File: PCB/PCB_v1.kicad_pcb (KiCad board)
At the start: 2 copper layers, 80 x 40 mm, 11 parts, among them J1 Accelerometer, J2 Flysky FS2A Receiver, J3 DC-DC, J4 Battery Left, J5 Battery Right, J6 ESC_Left, J7 ESC_Right, U1 Teensy4.0

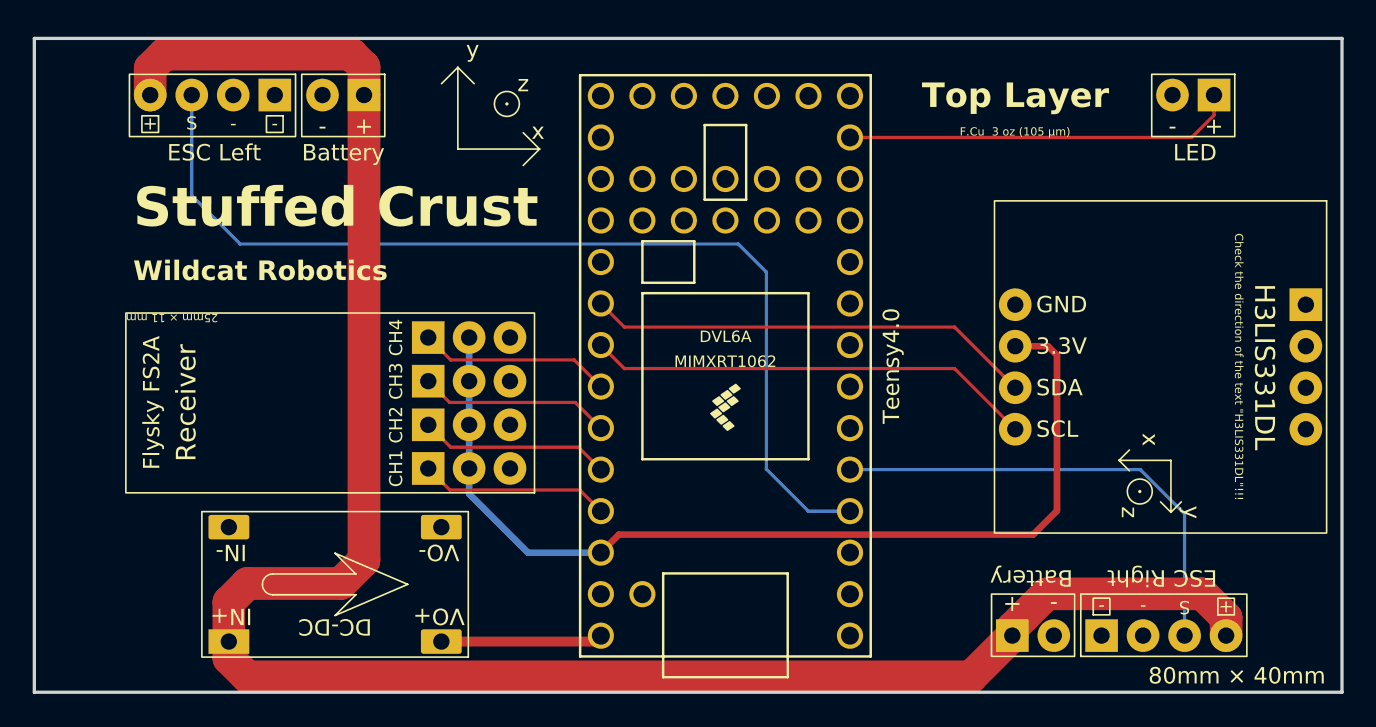
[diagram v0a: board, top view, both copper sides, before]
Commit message: Separate GND (for signal) and GND_BT (for high current); make bigger holes for high current wires
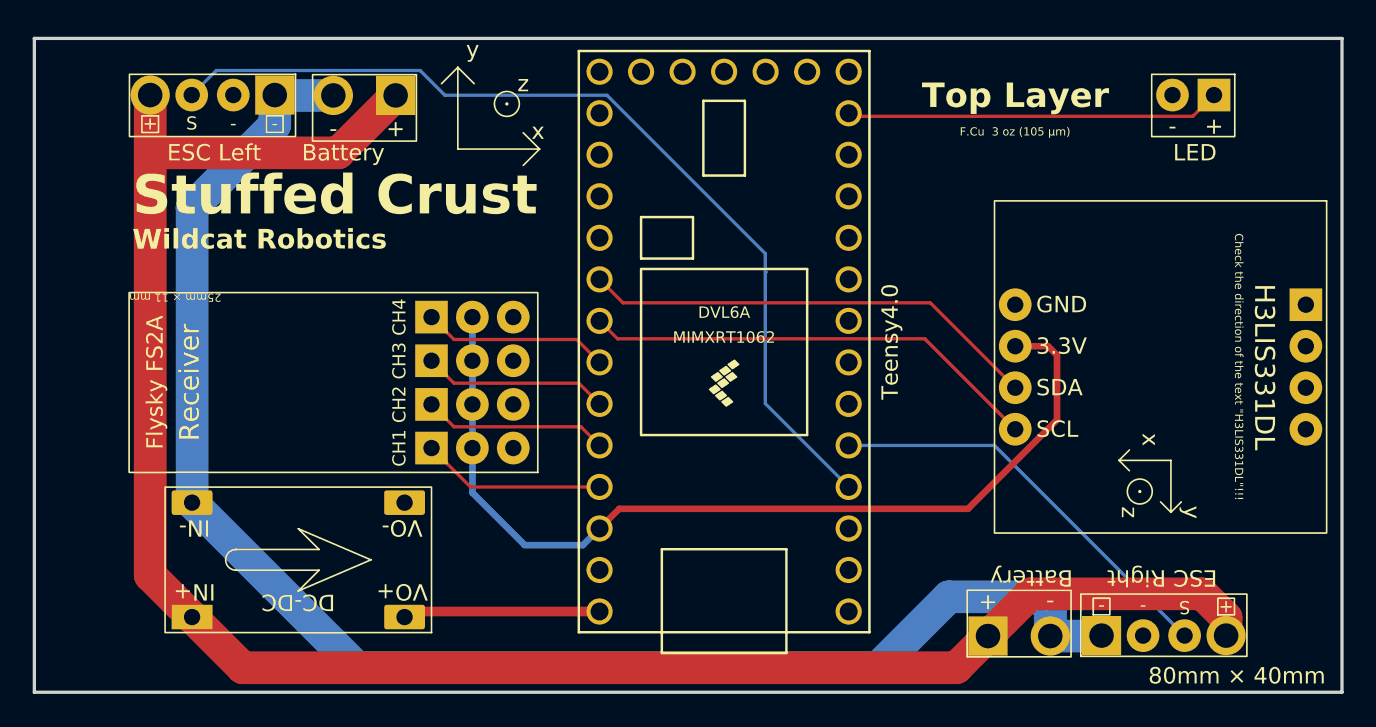
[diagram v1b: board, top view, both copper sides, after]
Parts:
- J4, J5: footprint Stuffed Crust:Battery_or_LED -> Stuffed Crust:Battery
- J8: renamed from Je; footprint Stuffed Crust:Battery_or_LED -> Stuffed Crust:LED
- moved J3 2.70 mm to (156.2, 91.9)
- moved J4 1.94 mm to (163.4, 62.2)
- moved J5 1.49 mm to (197.1, 97.8)
- moved U1 1.48 mm to (182.2, 78.5)
- moved J2 1.27 mm to (170.8, 86.5)
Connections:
- J3 pad 2: /GND -> /GND_BT
- J4 pad 2: /GND -> /GND_BT
- J5 pad 2: /GND -> /GND_BT
- J6 pad 1: /GND -> /GND_BT
- J7 pad 1: /GND -> /GND_BT
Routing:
- net /GND_BT: track 0.00 -> 94.3 mm
- net /12V: track 123.9 -> 117.6 mm
- net /S_ESC_Left_2: track 61.5 -> 56.8 mm
- net /S_ESC_Right_3: track 29.0 -> 25.4 mm
- net /3.3V: track 60.4 -> 57.8 mm
- net /5V: track 9.91 -> 12.1 mm
- net /LED: track 24.1 -> 23.0 mm
- net /SCL_19: track 27.5 -> 28.2 mm
- net /SDA_18: track 27.5 -> 28.2 mm
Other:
- board text added: "B.Cu 3 oz (105 μm)"
- board text removed: "B.Cu 1 oz (35 μm)"

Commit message: Fix the GND fill
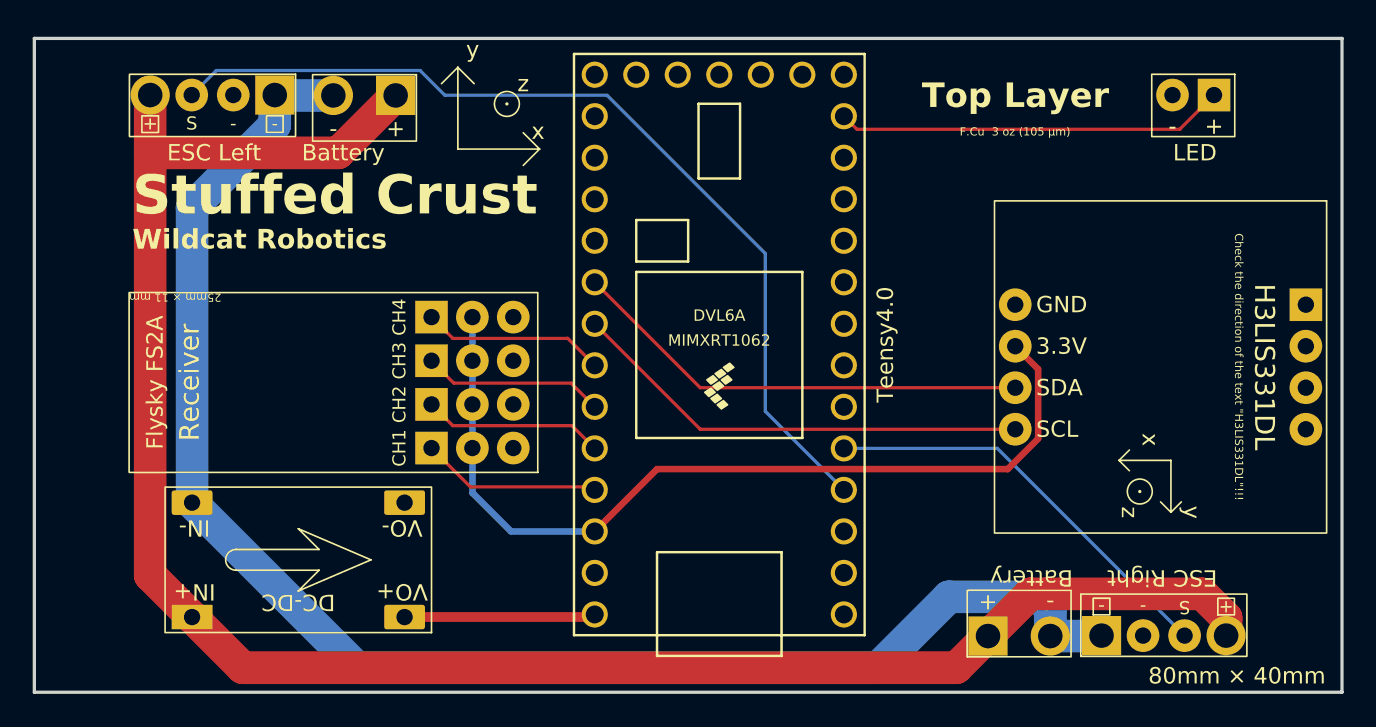
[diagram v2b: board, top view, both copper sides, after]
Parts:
- moved U1 0.35 mm to (181.9, 78.7)
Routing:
- net /3.3V: track 57.8 -> 54.9 mm
- net /LED: track 23.0 -> 24.1 mm
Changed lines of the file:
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@@
 	(footprint "Teensy:Teensy40"
 		(layer "F.Cu")
-		(at 182.2 78.55 90)
+		(at 181.905 78.73 90)
 		(property "Reference" "U1"
 			(at 0 -10.16 90)
@@
 	)
 	(segment
-		(start 197.122314 88.779)
-		(end 175.781 88.779)
+		(start 199.551314 86.35)
+		(end 201.411 84.490314)
 		(width 0.4)
 		(layer "F.Cu")
@@
 	)
 	(segment
-		(start 202.565 83.336314)
-		(end 197.122314 88.779)
+		(start 174.285 90.16)
+		(end 178.095 86.35)
 		(width 0.4)
 		(layer "F.Cu")
@@
 	)
 	(segment
-		(start 202.02 78.83)
-		(end 202.565 79.375)
+		(start 201.411 84.490314)
+		(end 201.411 80.231)
 		(width 0.4)
 		(layer "F.Cu")
@@
 	)
 	(segment
-		(start 202.565 79.375)
-		(end 202.565 83.336314)
+		(start 201.411 80.231)
+		(end 200.01 78.83)
 		(width 0.4)
 		(layer "F.Cu")
@@
 	)
 	(segment
-		(start 175.781 88.779)
-		(end 174.58 89.98)
+		(start 178.095 86.35)
+		(end 199.551314 86.35)
 		(width 0.4)
 		(layer "F.Cu")
@@
 	)
 	(segment
-		(start 200.01 78.83)
-		(end 202.02 78.83)
-		(width 0.4)
-		(layer "F.Cu")
-		(net 3)
-	)
-	(segment
-		(start 166.8 87.8)
-		(end 170 91)
+		(start 169.16 90.16)
+		(end 174.285 90.16)
 		(width 0.4)
 		(layer "B.Cu")
@@
 	)
 	(segment
-		(start 170 91)
-		(end 173.56 91)
+		(start 166.8 87.8)
+		(end 169.16 90.16)
 		(width 0.4)
 		(layer "B.Cu")
@@
 	)
 	(segment
-		(start 173.56 91)
-		(end 174.58 89.98)
-		(width 0.4)
-		(layer "B.Cu")
-		(net 3)
+		(start 180.735 83.91)
+		(end 174.285 77.46)
+		(width 0.2)
+		(layer "F.Cu")
+		(net 7)
 	)
 	(segment
 		(start 200.01 83.91)
-		(end 194.481 78.381)
+		(end 180.735 83.91)
 		(width 0.2)
 		(layer "F.Cu")
@@
 	)
 	(segment
-		(start 175.681 78.381)
-		(end 174.58 77.28)
-		(width 0.2)
-		(layer "F.Cu")
-		(net 7)
-	)
-	(segment
-		(start 194.481 78.381)
-		(end 175.681 78.381)
-		(width 0.2)
-		(layer "F.Cu")
-		(net 7)
-	)
-	(segment
-		(start 176.019 76.179)
-		(end 174.58 74.74)
+		(start 200.01 81.37)
+		(end 180.735 81.37)
 		(width 0.2)
 		(layer "F.Cu")
@@
 	)
 	(segment
-		(start 200.01 81.37)
-		(end 194.819 76.179)
+		(start 180.735 81.37)
+		(end 174.285 74.92)
 		(width 0.2)
 		(layer "F.Cu")
@@
 	)
 	(segment
-		(start 194.819 76.179)
-		(end 176.019 76.179)
-		(width 0.2)
-		(layer "F.Cu")
-		(net 8)
-	)
-	(segment
 		(start 165.669 81.089)
-		(end 173.309 81.089)
+		(end 172.834 81.089)
 		(width 0.2)
 		(layer "F.Cu")
@@
 	)
 	(segment
-		(start 173.309 81.089)
-		(end 174.58 82.36)
+		(start 172.834 81.089)
+		(end 174.285 82.54)
 		(width 0.2)
 		(layer "F.Cu")
@@
 	)
 	(segment
-		(start 165.669 83.759)
-		(end 173.439 83.759)
+		(start 165.601 83.691)
+		(end 172.896 83.691)
 		(width 0.2)
 		(layer "F.Cu")
@@
 	)
 	(segment
-		(start 173.439 83.759)
-		(end 174.58 84.9)
+		(start 172.896 83.691)
+		(end 174.285 85.08)
 		(width 0.2)
 		(layer "F.Cu")
@@
 	(segment
 		(start 164.3 82.39)
-		(end 165.669 83.759)
+		(end 165.601 83.691)
 		(width 0.2)
 		(layer "F.Cu")
@@
 	)
 	(segment
-		(start 165.669 78.419)
-		(end 173.179 78.419)
+		(start 172.636 78.351)
+		(end 174.285 80)
 		(width 0.2)
 		(layer "F.Cu")
@@
 	)
 	(segment
+		(start 165.601 78.351)
+		(end 172.636 78.351)
+		(width 0.2)
+		(layer "F.Cu")
+		(net 11)
+	)
+	(segment
 		(start 164.3 77.05)
-		(end 165.669 78.419)
-		(width 0.2)
-		(layer "F.Cu")
-		(net 11)
-	)
-	(segment
-		(start 173.179 78.419)
-		(end 174.58 79.82)
+		(end 165.601 78.351)
 		(width 0.2)
 		(layer "F.Cu")
@@
 	)
 	(segment
-		(start 174.58 95.06)
-		(end 162.99 95.06)
+		(start 174.125 95.4)
+		(end 174.285 95.24)
+		(width 0.2)
+		(layer "F.Cu")
+		(net 14)
+	)
+	(segment
+		(start 162.65 95.4)
+		(end 174.125 95.4)
 		(width 0.6)
 		(layer "F.Cu")
@@
 	)
 	(segment
-		(start 184.72 82.34)
-		(end 189.82 87.44)
+		(start 184.72 73.16295)
+		(end 184.72 82.815)
 		(width 0.2)
 		(layer "B.Cu")
@@
 	)
 	(segment
-		(start 175.03605 63.479)
-		(end 165.116 63.479)
+		(start 151.131 61.964)
+		(end 163.601 61.964)
 		(width 0.2)
 		(layer "B.Cu")
@@
 	)
 	(segment
-		(start 165.116 63.479)
-		(end 163.601 61.964)
+		(start 149.63 63.465)
+		(end 151.131 61.964)
 		(width 0.2)
 		(layer "B.Cu")
@@
 	)
 	(segment
-		(start 163.601 61.964)
-		(end 151.131 61.964)
+		(start 165.116 63.479)
+		(end 175.03605 63.479)
 		(width 0.2)
 		(layer "B.Cu")
@@
 	)
 	(segment
-		(start 184.72 82.34)
-		(end 184.72 73.16295)
+		(start 163.601 61.964)
+		(end 165.116 63.479)
 		(width 0.2)
 		(layer "B.Cu")
@@
 	)
 	(segment
+		(start 184.72 82.815)
+		(end 189.525 87.62)
+		(width 0.2)
+		(layer "B.Cu")
+		(net 15)
+	)
+	(segment
+		(start 175.03605 63.479)
+		(end 184.72 73.16295)
+		(width 0.2)
+		(layer "B.Cu")
+		(net 15)
+	)
+	(segment
 		(start 184.72 74.23)
 		(end 184.785 74.295)
@@
 	)
 	(segment
-		(start 184.72 73.16295)
-		(end 175.03605 63.479)
-		(width 0.2)
-		(layer "B.Cu")
-		(net 15)
-	)
-	(segment
-		(start 151.131 61.964)
-		(end 149.63 63.465)
-		(width 0.2)
-		(layer "B.Cu")
-		(net 15)
-	)
-	(segment
-		(start 198.735 84.9)
-		(end 210.37 96.535)
+		(start 189.525 85.08)
+		(end 198.915 85.08)
 		(width 0.2)
 		(layer "B.Cu")
@@
 	)
 	(segment
-		(start 189.82 84.9)
-		(end 198.735 84.9)
+		(start 198.915 85.08)
+		(end 210.37 96.535)
 		(width 0.2)
 		(layer "B.Cu")
@@
 	)
 	(segment
-		(start 210.869 64.766)
-		(end 190.006 64.766)
+		(start 190.324999 65.559999)
+		(end 210.075001 65.559999)
 		(width 0.2)
 		(layer "F.Cu")
@@
 	)
 	(segment
-		(start 212.17 63.465)
-		(end 210.869 64.766)
-		(width 0.2)
-		(layer "F.Cu")
+		(start 189.525 64.76)
+		(end 190.324999 65.559999)
+		(width 0.2)
+		(layer "F.Cu")
+		(net 17)
+	)
+	(segment
+		(start 210.075001 65.559999)
+		(end 212.17 63.465)
+		(width 0.2)
+		(layer "F.Cu")

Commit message: Remove the small "GND" from ESC
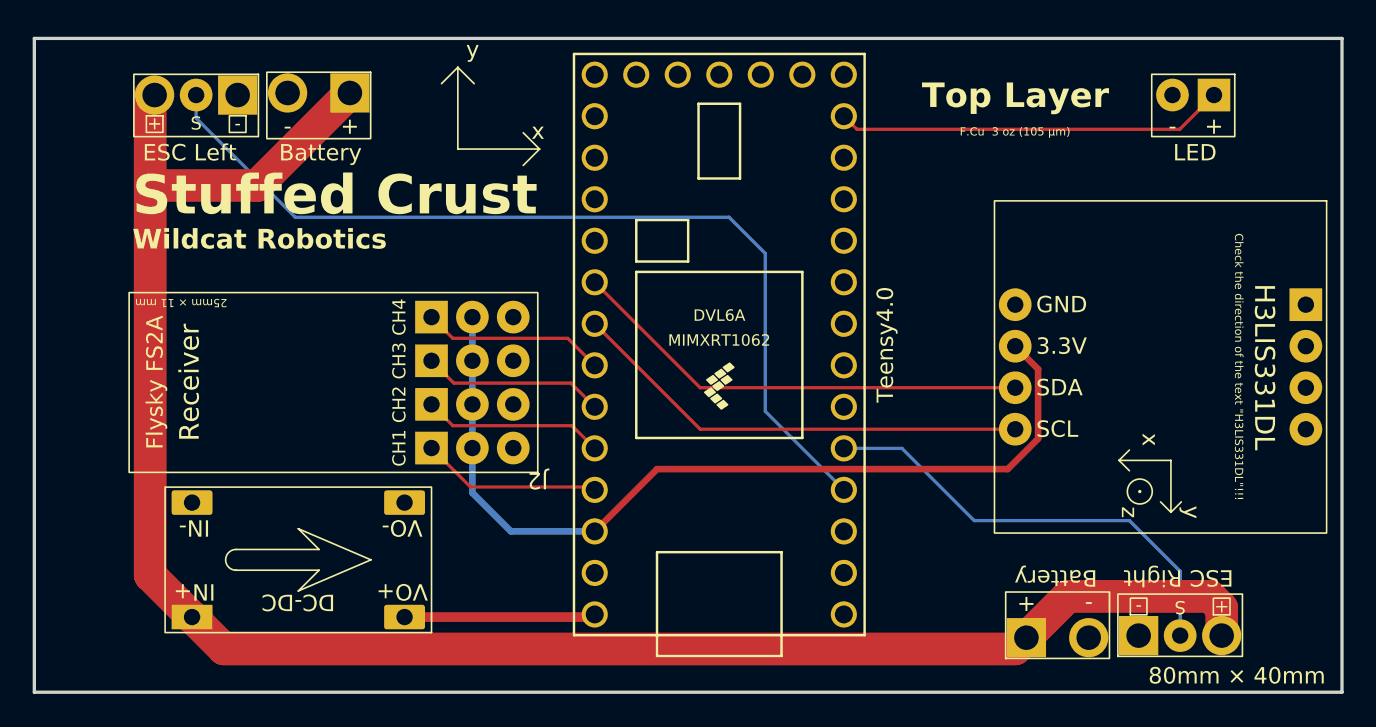
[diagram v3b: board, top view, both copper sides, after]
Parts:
- removed ?: , clipboard:2c392293-ef90-46e6-a046-d4cdf45f70c2
- removed ?: , clipboard:1efe44ad-3118-4d5e-9bd0-140298458513
- moved J4 2.80 mm to (160.6, 62.1)
- moved J5 2.35 mm to (199.4, 97.9)
- moved J6 2.27 mm to (153.7, 62.2)
- moved J7 2.27 mm to (206.3, 97.8)
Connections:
- J3 pad 2: /GND_BT -> /GND
- J4 pad 2: /GND_BT -> /GND
- J5 pad 2: /GND_BT -> /GND
- J6 pad 1: /GND_BT -> /GND
- J6 pad 2: /GND -> /S_ESC_Left_2
- J6 pad 3: /S_ESC_Left_2 -> /12V
- J7 pad 1: /GND_BT -> /GND
- J7 pad 2: /GND -> /S_ESC_Right_3
- J7 pad 3: /S_ESC_Right_3 -> /12V
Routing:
- net /GND_BT: track 94.3 -> 0.00 mm
- net /12V: track 117.6 -> 114.7 mm
- net /S_ESC_Right_3: track 25.6 -> 27.6 mm
- net /S_ESC_Left_2: track 56.9 -> 56.1 mm

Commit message: Only Keep S Pins for ESCs
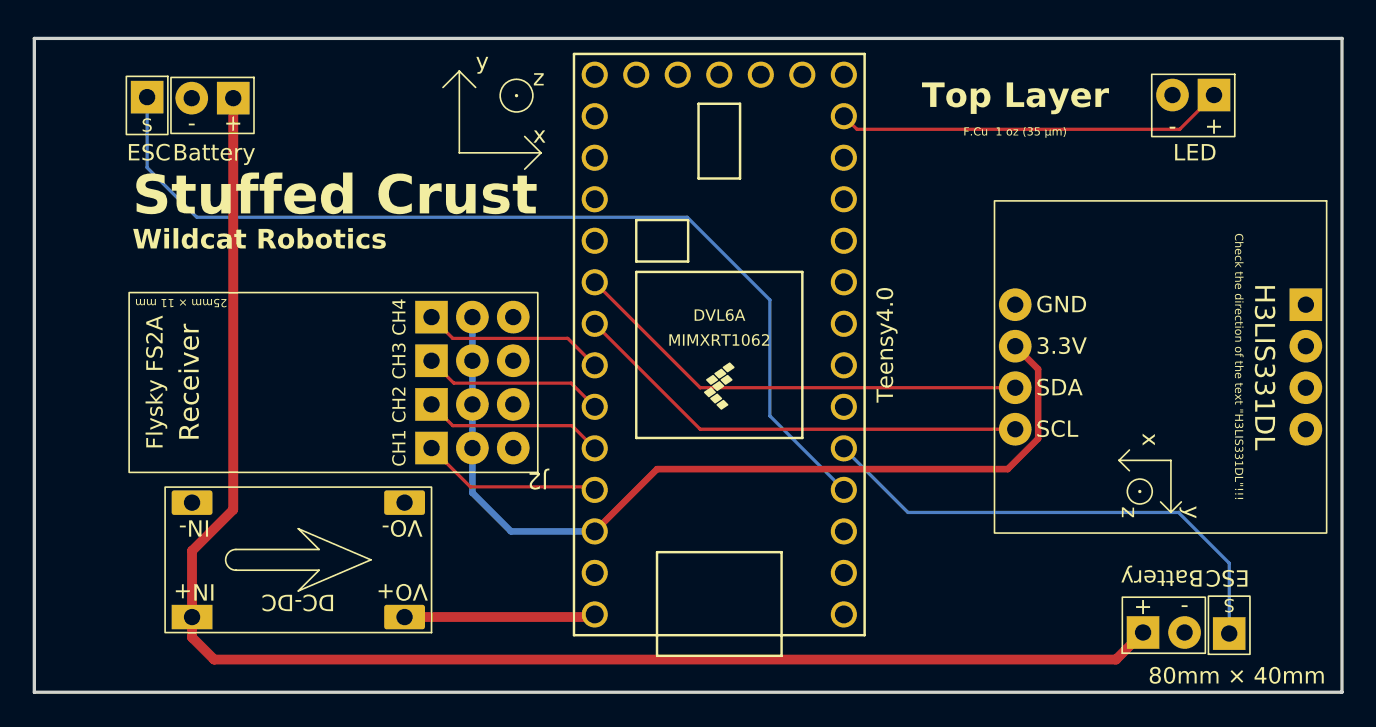
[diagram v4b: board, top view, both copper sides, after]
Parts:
- moved J4 7.14 mm to (153.4, 62.4)
- moved J5 7.14 mm to (206.6, 97.6)
- moved J6 5.54 mm to (148.2, 62.3)
- moved J7 5.54 mm to (211.8, 97.7)
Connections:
- J6 pad 1: /GND -> /S_ESC_Left_2
- J7 pad 1: /GND -> /S_ESC_Right_3
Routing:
- net /12V: track 114.7 -> 93.5 mm
- net /S_ESC_Right_3: track 27.6 -> 30.8 mm
- net /S_ESC_Left_2: track 56.1 -> 59.3 mm
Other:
- board text added: "B.Cu 1 oz (35 μm)"
- board text added: "ESC"
- board text added: "F.Cu 1 oz (35 μm)"
- board text added: "z"
- board text removed: "B.Cu 3 oz (105 μm)"
- board text removed: "ESC Left"
- board text removed: "ESC Right"
- board text removed: "F.Cu 3 oz (105 μm)"
